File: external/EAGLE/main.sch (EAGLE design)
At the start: 7 parts, among them IC1 AD590ZR, IC2 L293D, IC5 AT24CP, X2 332-02, X3 5566-16

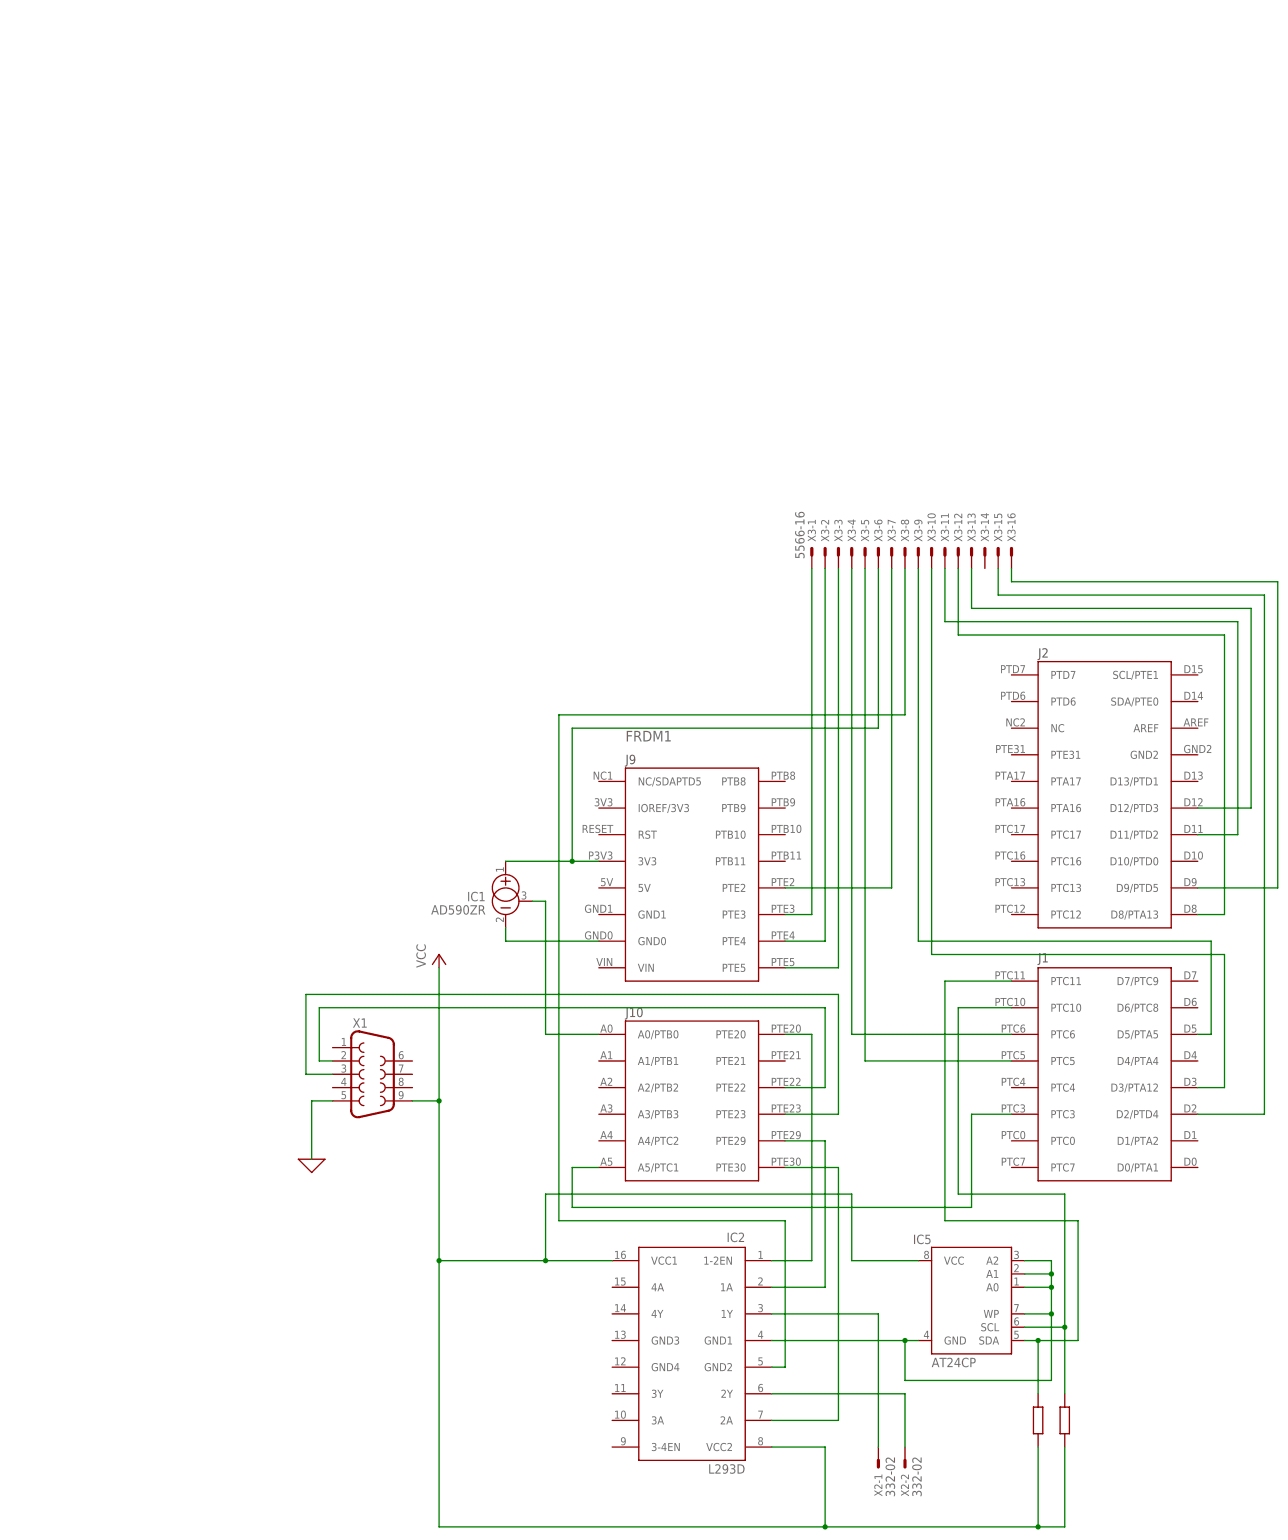
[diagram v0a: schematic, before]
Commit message: Updating the schematic
The schematic was designed entirely by Daniela.
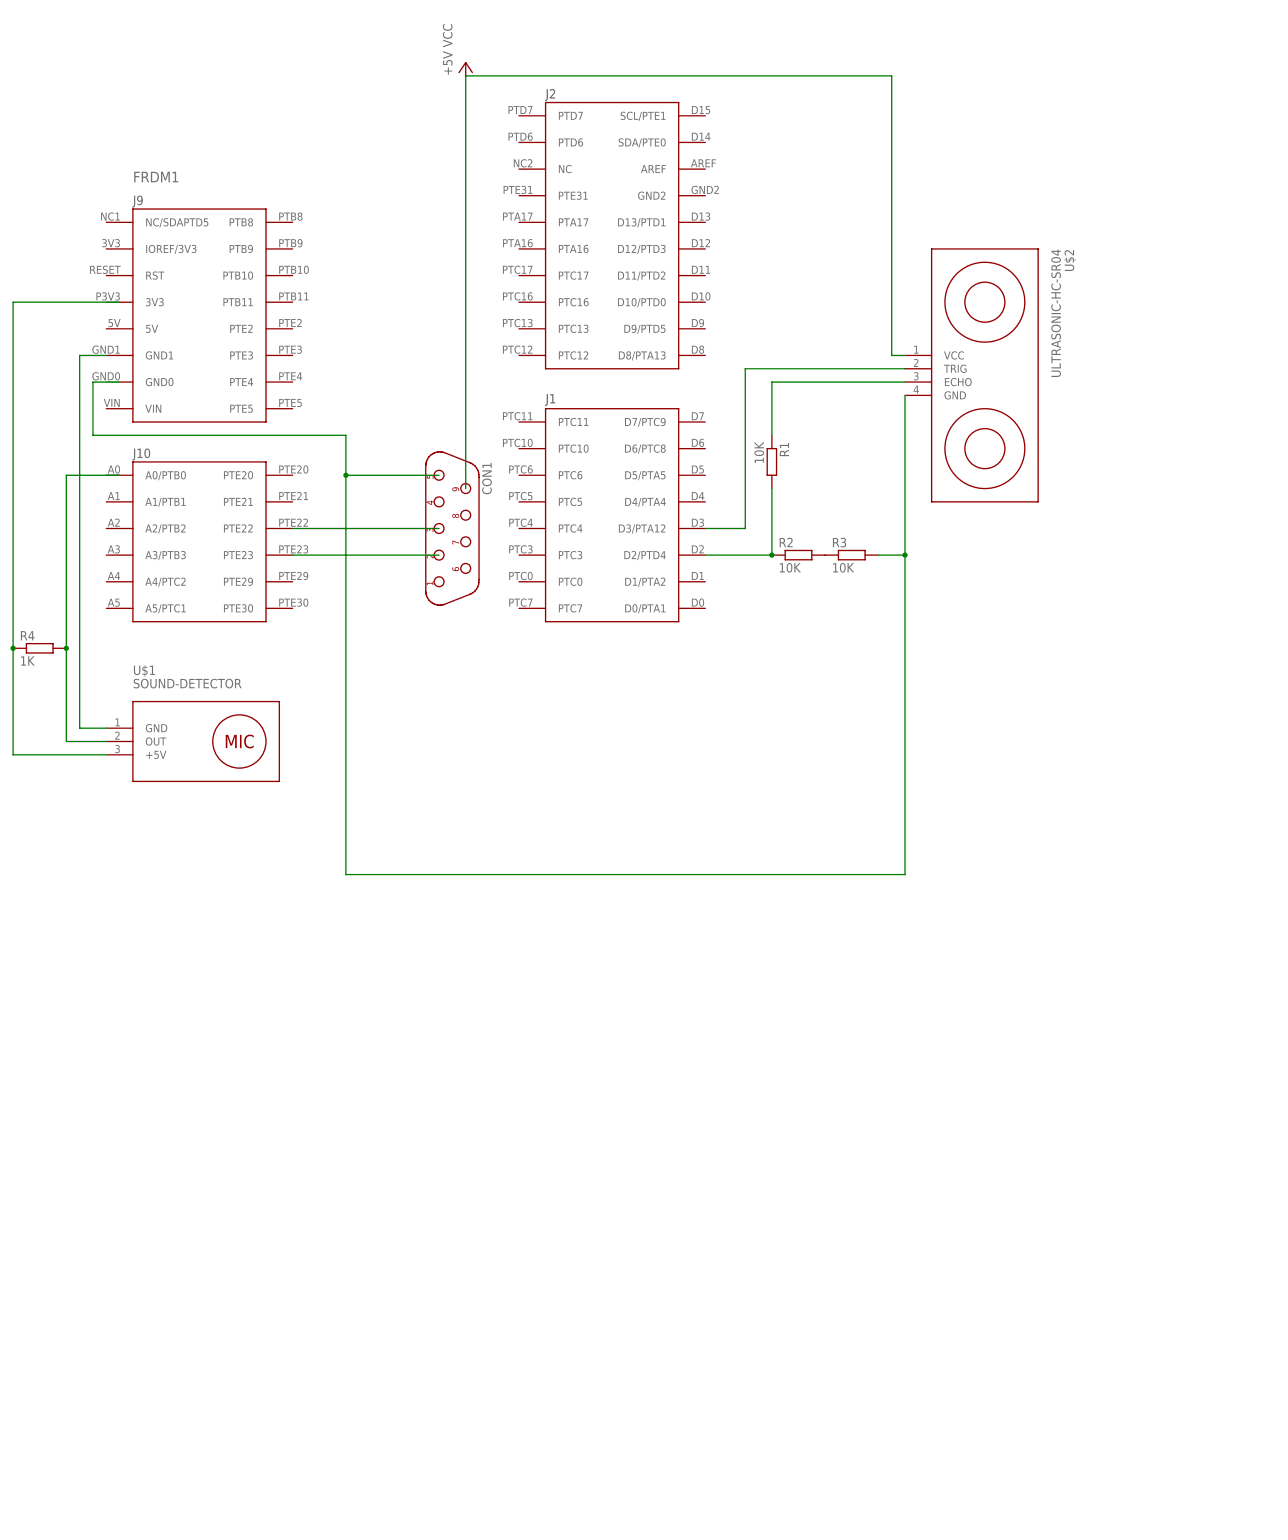
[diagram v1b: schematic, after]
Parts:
- removed IC1: AD590ZR, linear:AD590ZR
- removed IC2: L293D, st-microelectronics:L293D
- removed IC5: AT24CP, atmel:AT24CP
- removed X1: (no value), con-subd:F09D
- removed X2: 332-02, con-garry:332-02
- removed X3: 5566-16, con-molex:5566-16
- added CON1: (no value), connect:DB9F
- added R1, R2, R3: 10K, resistor:R-EU_0204/7
- added R4: 1K, resistor:R-EU_0204/7
- added U$1: SOUND-DETECTOR, diy-modules:SOUND-DETECTOR
- added U$2: ULTRASONIC-HC-SR04, diy-modules:ULTRASONIC-HC-SR04
- FRDM1: device FRDM:FRDM-KL25ZNORMAL -> Freedom:FRDM-KL25ZNORMAL
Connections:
- removed net 0: X1.5
- removed net N$1: FRDM1.PTE22, X1.2
- removed net N$11: FRDM1.GND0, IC1.-, IC2.GND1, IC2.GND2, IC5.A0, IC5.A1, IC5.A2, IC5.GND, IC5.WP, X3-8.S
- removed net N$13: FRDM1.PTE5, X3-3.S
- removed net N$14: FRDM1.PTE4, X3-2.S
- removed net N$15: FRDM1.PTE2, X3-7.S
- removed net N$16: FRDM1.PTC6, X3-4.S
- removed net N$17: FRDM1.PTC5, X3-5.S
- removed net N$18: FRDM1.D5/PTA5, X3-9.S
- removed net N$19: FRDM1.D3/PTA12, X3-10.S
- removed net N$20: FRDM1.D8/PTA13, X3-12.S
- removed net N$21: FRDM1.D11/PTD2, X3-11.S
- removed net N$22: FRDM1.D12/PTD3, X3-13.S
- removed net N$23: FRDM1.D2/PTD4, X3-15.S
- removed net N$24: FRDM1.D9/PTD5, X3-16.S
- removed net N$27: FRDM1.PTC10, IC5.SCL
- removed net N$28: FRDM1.PTC11, IC5.SDA
- net N$10: now also CON1.3, FRDM1.PTE22; no longer IC2.2Y, X2-2.S
- net N$12: now also CON1.2, FRDM1.PTE23; no longer FRDM1.PTE3, X3-1.S
- net N$2: now also FRDM1.D3/PTA12, U$2.TRIG; no longer FRDM1.PTE23, X1.3
- net N$3: now also R1.1, U$2.ECHO; no longer FRDM1.A5/PTC1, FRDM1.PTC3
- net N$4: now also FRDM1.D2/PTD4, R1.2, R2.1; no longer FRDM1.A0/PTB0, IC1.CAN
- net N$5: now also R2.2, R3.1; no longer IC2.1Y, X2-1.S
- net N$6: now also CON1.5, R3.2, U$2.GND; no longer FRDM1.3V3, IC1.+, X3-6.S
- net N$7: now also R4.2, U$1.OUT; no longer FRDM1.PTE20, IC2.1-2EN
- net N$8: now also R4.1, U$1.+5V; no longer FRDM1.PTE29, IC2.1A
- net N$9: now also FRDM1.GND1, U$1.GND; no longer FRDM1.PTE30, IC2.2A
- net VCC: now also CON1.9, U$2.VCC; no longer IC2.VCC1, IC2.VCC2, IC5.VCC, X1.9
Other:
- moved on the sheet: FRDM1
